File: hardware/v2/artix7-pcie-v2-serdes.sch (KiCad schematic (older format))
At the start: 23 parts, among them J4 USB3_A, J5 USB3_A_AS_PCIE, U1 XC7A75T-FGG484

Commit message: v2 hardware: add Digikey part numbers to schematic and generate bom
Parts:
- C19, C34: Vendor (none) -> 490-5915-1-ND
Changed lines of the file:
@@
 F 2 "tom-passives:C_0402_1005Metric" H 9638 5350 30  0001 C CNN
 F 3 "" H 9600 5500 60  0001 C CNN
+F 4 "490-5915-1-ND" H 9600 5500 50  0001 C CNN "Vendor"
 	1    9600 5500
 	1    0    0    -1
@@
 F 2 "tom-passives:C_0402_1005Metric" H 3338 5350 30  0001 C CNN
 F 3 "" H 3300 5500 60  0001 C CNN
+F 4 "490-5915-1-ND" H 3300 5500 50  0001 C CNN "Vendor"
 	1    3300 5500
 	1    0    0    -1

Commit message: hardware: add USB 3.0 connector digikey part number
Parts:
- J4, J5: Digikey (none) -> 2057-USB-A3-S-RA-ND
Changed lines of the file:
@@
 F 2 "tom-connectors:USB3_A_Aliexpress" H 2650 2350 50  0001 C CNN
 F 3 "~" H 2650 2350 50  0001 C CNN
+F 4 "2057-USB-A3-S-RA-ND" H 2500 2250 50  0001 C CNN "Digikey"
 	1    2500 2250
 	1    0    0    -1
@@
 F 2 "tom-connectors:USB3_A_Aliexpress" H 2650 4600 50  0001 C CNN
 F 3 "~" H 2650 4600 50  0001 C CNN
+F 4 "2057-USB-A3-S-RA-ND" H 2500 4500 50  0001 C CNN "Digikey"
 	1    2500 4500
 	1    0    0    -1

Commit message: v2 hardware: aug2020 pcb updates
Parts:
- removed R42, R44: DNP, tom-passives:R_0402_1005Metric_NoPaste, symbol tom-passives:R
- removed R43, R45: 0R, tom-passives:R_0402_1005Metric, symbol tom-passives:R
- added C3, C4: 0.1uF/6.3V/X5R, tom-passives:C_0402_1005Metric, symbol tom-passives:C
- R26, R27: value 0R -> 270R/5%
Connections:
- net S2_DRAIN is gone; now on net GND: J5.7 (DRAIN)
- net S2_GND is gone; now on net S2_PERST: J5.4 (GND)
- net GND: now also C3.2, C4.2
- net S2_RX_N: now also U1.B10 (MGTPRXP2_216); no longer U1.A10 (MGTPRXN2_216)
- net S2_RX_P: now also U1.A10 (MGTPRXN2_216); no longer U1.B10 (MGTPRXP2_216)
- net at J4.10 (SHIELD), R26.1: now also C3.1
- net at J5.10 (SHIELD), R27.1: now also C4.1
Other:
- note added: "P/N reversal on MGT2 RX"
- moved on the sheet: R26, R27
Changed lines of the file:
@@
 L tom-passives:R R26
 U 1 1 5EACE9C5
-P 2050 3050
-F 0 "R26" V 1865 3050 40  0000 C CNN
-F 1 "0R" V 1941 3050 40  0000 C CNN
-F 2 "tom-passives:R_0402_1005Metric" V 1980 3050 30  0001 C CNN
-F 3 "" H 2050 3050 30  0001 C CNN
-	1    2050 3050
-	0    1    1    0
+P 1500 3050
+F 0 "R26" V 1315 3050 40  0000 C CNN
+F 1 "270R/5%" V 1391 3050 40  0000 C CNN
+F 2 "tom-passives:R_0402_1005Metric" V 1430 3050 30  0001 C CNN
+F 3 "" H 1500 3050 30  0001 C CNN
+	1    1500 3050
+	0    1    -1   0
 $EndComp
 Wire Wire Line
@@
 L power:GND #PWR058
 U 1 1 5EACF99A
-P 1800 3050
-F 0 "#PWR058" H 1800 2800 50  0001 C CNN
-F 1 "GND" H 1805 2877 50  0000 C CNN
-F 2 "" H 1800 3050 50  0001 C CNN
-F 3 "" H 1800 3050 50  0001 C CNN
-	1    1800 3050
+P 1100 3050
+F 0 "#PWR058" H 1100 2800 50  0001 C CNN
+F 1 "GND" H 1105 2877 50  0000 C CNN
+F 2 "" H 1100 3050 50  0001 C CNN
+F 3 "" H 1100 3050 50  0001 C CNN
+	1    1100 3050
 	1    0    0    -1
 $EndComp
 Text HLabel 1700 5950 0    50   Output ~ 0
 S2_PERST
-Wire Wire Line
-	2300 5200 2300 5350
 $Comp
 L power:GND #PWR059
 U 1 1 5EAD2F17
-P 1800 5350
-F 0 "#PWR059" H 1800 5100 50  0001 C CNN
-F 1 "GND" H 1805 5177 50  0000 C CNN
-F 2 "" H 1800 5350 50  0001 C CNN
-F 3 "" H 1800 5350 50  0001 C CNN
-	1    1800 5350
+P 1700 5650
+F 0 "#PWR059" H 1700 5400 50  0001 C CNN
+F 1 "GND" H 1705 5477 50  0000 C CNN
+F 2 "" H 1700 5650 50  0001 C CNN
+F 3 "" H 1700 5650 50  0001 C CNN
+	1    1700 5650
 	1    0    0    -1
 $EndComp
@@
 L tom-passives:R R27
 U 1 1 5EAD1FF6
-P 2050 5350
-F 0 "R27" V 1865 5350 40  0000 C CNN
-F 1 "0R" V 1941 5350 40  0000 C CNN
-F 2 "tom-passives:R_0402_1005Metric" V 1980 5350 30  0001 C CNN
-F 3 "" H 2050 5350 30  0001 C CNN
-	1    2050 5350
+P 2000 5350
+F 0 "R27" V 1815 5350 40  0000 C CNN
+F 1 "270R/5%" V 1891 5350 40  0000 C CNN
+F 2 "tom-passives:R_0402_1005Metric" V 1930 5350 30  0001 C CNN
+F 3 "" H 2000 5350 30  0001 C CNN
+	1    2000 5350
 	0    1    1    0
-$EndComp
-$Comp
-L power:GND #PWR061
-U 1 1 5EACBD31
-P 3000 5950
-F 0 "#PWR061" H 3000 5700 50  0001 C CNN
-F 1 "GND" H 3005 5777 50  0000 C CNN
-F 2 "" H 3000 5950 50  0001 C CNN
-F 3 "" H 3000 5950 50  0001 C CNN
-	1    3000 5950
-	1    0    0    -1
 $EndComp
 Wire Wire Line
@@
 	1    0    0    -1
 $EndComp
-$Comp
-L tom-passives:R R44
-U 1 1 5F029E9A
-P 2750 5950
-F 0 "R44" V 2565 5950 40  0000 C CNN
-F 1 "DNP" V 2641 5950 40  0000 C CNN
-F 2 "tom-passives:R_0402_1005Metric_NoPaste" V 2680 5950 30  0001 C CNN
-F 3 "" H 2750 5950 30  0001 C CNN
-	1    2750 5950
-	0    1    1    0
-$EndComp
-$Comp
-L tom-passives:R R43
-U 1 1 5F02A201
-P 2150 5950
-F 0 "R43" V 1965 5950 40  0000 C CNN
-F 1 "0R" V 2041 5950 40  0000 C CNN
-F 2 "tom-passives:R_0402_1005Metric" V 2080 5950 30  0001 C CNN
-F 3 "" H 2150 5950 30  0001 C CNN
-	1    2150 5950
-	0    1    1    0
-$EndComp
 Wire Wire Line
 	2500 5200 2500 5950
 Wire Wire Line
-	2500 5950 2400 5950
-Connection ~ 2500 5950
-Wire Wire Line
-	1700 5950 1900 5950
-$Comp
-L tom-passives:R R42
-U 1 1 5F0598E8
-P 2150 5650
-F 0 "R42" V 1965 5650 40  0000 C CNN
-F 1 "DNP" V 2041 5650 40  0000 C CNN
-F 2 "tom-passives:R_0402_1005Metric_NoPaste" V 2080 5650 30  0001 C CNN
-F 3 "" H 2150 5650 30  0001 C CNN
-	1    2150 5650
-	0    1    1    0
-$EndComp
-Wire Wire Line
-	1900 5650 1900 5950
-Connection ~ 1900 5950
-Wire Wire Line
 	2400 5200 2400 5650
-$Comp
-L tom-passives:R R45
-U 1 1 5F07398D
-P 2850 5650
-F 0 "R45" V 2665 5650 40  0000 C CNN
-F 1 "0R" V 2741 5650 40  0000 C CNN
-F 2 "tom-passives:R_0402_1005Metric" V 2780 5650 30  0001 C CNN
-F 3 "" H 2850 5650 30  0001 C CNN
-	1    2850 5650
-	0    1    1    0
-$EndComp
 $Comp
 L power:GND #PWR035
 U 1 1 5F073E12
-P 3100 5650
-F 0 "#PWR035" H 3100 5400 50  0001 C CNN
-F 1 "GND" H 3105 5477 50  0000 C CNN
-F 2 "" H 3100 5650 50  0001 C CNN
-F 3 "" H 3100 5650 50  0001 C CNN
-	1    3100 5650
-	1    0    0    -1
-$EndComp
-Wire Wire Line
-	2600 5650 2400 5650
-Connection ~ 2400 5650
-$Comp
-L power:PWR_FLAG #FLG0114
-U 1 1 5F118316
-P 2600 5650
-F 0 "#FLG0114" H 2600 5725 50  0001 C CNN
-F 1 "PWR_FLAG" V 2600 5950 50  0000 C CNN
-F 2 "" H 2600 5650 50  0001 C CNN
-F 3 "~" H 2600 5650 50  0001 C CNN
-	1    2600 5650
-	1    0    0    -1
-$EndComp
-Connection ~ 2600 5650
-$Comp
-L power:PWR_FLAG #FLG0115
-U 1 1 5F11842A
-P 2400 5950
-F 0 "#FLG0115" H 2400 6025 50  0001 C CNN
-F 1 "PWR_FLAG" H 2400 6123 50  0000 C CNN
-F 2 "" H 2400 5950 50  0001 C CNN
-F 3 "~" H 2400 5950 50  0001 C CNN
-	1    2400 5950
-	-1   0    0    1
-$EndComp
-Connection ~ 2400 5950
+P 2400 5650
+F 0 "#PWR035" H 2400 5400 50  0001 C CNN
+F 1 "GND" H 2405 5477 50  0000 C CNN
+F 2 "" H 2400 5650 50  0001 C CNN
+F 3 "" H 2400 5650 50  0001 C CNN
+	1    2400 5650
+	1    0    0    -1
+$EndComp
 NoConn ~ 7250 2000
 NoConn ~ 7250 2100
-Wire Wire Line
-	4300 3200 7250 3200
-Wire Wire Line
-	7250 3100 4400 3100
 Wire Wire Line
 	7250 2300 5400 2300
@@
 Wire Wire Line
 	8900 5700 9100 5700
-Text Label 2500 5600 1    50   ~ 0
-S2_GND
-Text Label 2400 5600 1    50   ~ 0
-S2_DRAIN
 Wire Wire Line
 	3100 3500 1900 3500
@@
 	7150 3000 7150 3300
 Wire Wire Line
-	4300 3200 4300 4600
-Wire Wire Line
-	4400 3100 4400 4700
+	4300 3100 4300 4600
+Wire Wire Line
+	4400 3200 4400 4700
 Wire Wire Line
 	7250 3300 7150 3300
@@
 NoConn ~ 7250 2400
 NoConn ~ 7250 2500
+Wire Wire Line
+	1700 5950 2500 5950
+Wire Wire Line
+	4400 3200 7250 3200
+Wire Wire Line
+	7250 3100 4300 3100
+Text Label 6650 3100 0    50   ~ 0
+S2_RX_N
+Text Label 6650 3200 0    50   ~ 0
+S2_RX_P
+Text Notes 6100 3000 0    50   ~ 0
+P/N reversal on MGT2 RX
+$Comp
+L tom-passives:C C4
+U 1 1 5F73BB56
+P 2000 5550
+F 0 "C4" V 2100 5400 40  0000 L CNN
+F 1 "0.1uF/6.3V/X5R" V 2200 5300 40  0000 L CNN
+F 2 "tom-passives:C_0402_1005Metric" H 2038 5400 30  0001 C CNN
+F 3 "" H 2000 5550 60  0001 C CNN
+	1    2000 5550
+	0    1    1    0
+$EndComp
+Wire Wire Line
+	2300 5550 2200 5550
+Wire Wire Line
+	1750 5350 1700 5350
+Wire Wire Line
+	1700 5350 1700 5550
+Wire Wire Line
+	1800 5550 1700 5550
+Connection ~ 1700 5550
+Wire Wire Line
+	1700 5550 1700 5650
+Wire Wire Line
+	2300 5200 2300 5350
+Wire Wire Line
+	2250 5350 2300 5350
+Connection ~ 2300 5350
+Wire Wire Line
+	2300 5350 2300 5550
+Wire Wire Line
+	2300 3050 1750 3050
+Wire Wire Line
+	1700 2750 1750 2750
+Wire Wire Line
+	1750 2750 1750 3050
+Connection ~ 1750 3050
+Wire Wire Line
+	1300 2750 1250 2750
+Wire Wire Line
+	1250 2750 1250 3050
+Wire Wire Line
+	1250 3050 1100 3050
+Connection ~ 1250 3050
+$Comp
+L tom-passives:C C3
+U 1 1 5F763D00
+P 1500 2750
+F 0 "C3" V 1600 2600 40  0000 L CNN
+F 1 "0.1uF/6.3V/X5R" V 1700 2500 40  0000 L CNN
+F 2 "tom-passives:C_0402_1005Metric" H 1538 2600 30  0001 C CNN
+F 3 "" H 1500 2750 60  0001 C CNN
+	1    1500 2750
+	0    1    -1   0
+$EndComp
 $EndSCHEMATC

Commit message: v2 hardware: Aug2020/rc2 version - flip tx/rx pairs on s2 - add lcsc part numbers
rc2 errata schematic
- change serial port connector to add +3.3V ? (8-pin)(NO)
- add test points for flash pre-programming
- smaller package on input direction diodes (NO)
- bom dupe errors
- remove all p/s 0R bringup parts
- optimise bom (use 1.5k for led, 10k/4.7k for i2c pullups)
- done led is bright (change to 4.7k)
- improve shield grounding with RC
- check actual values of RGB resistors
- remove caps from clock inputs

rc2 errata pcb
- no gnd marking on serial port connector pins
- change serial port connector to add +3.3V ? (8-pin) (NO)
- no test points for flash pre-programming
- missing caps on xtal? (No but select xtal carefully)
- Cfg sel pins on clock chip?
- No silk on test points
- No +/- pair numbering on silk
- vcc test points for clk pre-programming? (or use bootloader)
- random silk circle under S2
- smaller package on input direction diodes (NO)
- no polarity on 100uF tantalum
- some via in or close to pads
- wrong button package (change from feather to chinese)
- gnd/vcc labels swapped at high end of J2
- clock chip OUT0_SEL_I2CB needs to be tied high after programming
- check teardrops
- power diode footprint marking reverse
- LEDs use cap footprint
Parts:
- C19, C34: LCSC (none) -> C23733
- C20, C21, C22, C24, C26, C28, C3, C30, C32, C33, C4, C47, C48: LCSC (none) -> C1525
- J4, J5, U1: LCSC (none) -> DNP
- R26, R27: LCSC (none) -> C25099
- R28: LCSC (none) -> C25076
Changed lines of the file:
@@
 F 2 "artix7-pcie-v2:Xilinx_FGG484" H 8750 2900 50  0001 C CNN
 F 3 "" H 8750 2900 50  0000 C CNN
+F 4 "DNP" H 8750 2900 50  0001 C CNN "LCSC"
 	4    8750 2900
 	1    0    0    -1
@@
 F 3 "~" H 2650 2350 50  0001 C CNN
 F 4 "2057-USB-A3-S-RA-ND" H 2500 2250 50  0001 C CNN "Digikey"
+F 5 "DNP" H 2500 2250 50  0001 C CNN "LCSC"
 	1    2500 2250
 	1    0    0    -1
@@
 F 2 "tom-passives:C_0402_1005Metric" H 5738 1650 30  0001 C CNN
 F 3 "" H 5700 1800 60  0001 C CNN
+F 4 "C1525" H 5700 1800 50  0001 C CNN "LCSC"
 	1    5700 1800
 	0    1    1    0
@@
 F 2 "tom-passives:C_0402_1005Metric" H 6238 1750 30  0001 C CNN
 F 3 "" H 6200 1900 60  0001 C CNN
+F 4 "C1525" H 6200 1900 50  0001 C CNN "LCSC"
 	1    6200 1900
 	0    1    1    0
@@
 F 2 "tom-passives:R_0402_1005Metric" V 1430 3050 30  0001 C CNN
 F 3 "" H 1500 3050 30  0001 C CNN
+F 4 "C25099" H 1500 3050 50  0001 C CNN "LCSC"
 	1    1500 3050
 	0    1    -1   0
@@
 F 2 "tom-passives:R_0402_1005Metric" V 1930 5350 30  0001 C CNN
 F 3 "" H 2000 5350 30  0001 C CNN
+F 4 "C25099" H 2000 5350 50  0001 C CNN "LCSC"
 	1    2000 5350
 	0    1    1    0
@@
 F 2 "artix7-pcie-v2:Xilinx_FGG484" H 6550 5700 50  0001 C CNN
 F 3 "" H 6550 5700 50  0000 C CNN
+F 4 "DNP" H 6550 5700 50  0001 C CNN "LCSC"
 	5    6550 5700
 	1    0    0    -1
@@
 F 2 "tom-passives:R_0402_1005Metric" V 8280 6000 30  0001 C CNN
 F 3 "" H 8350 6000 30  0001 C CNN
+F 4 "C25076" H 8350 6000 50  0001 C CNN "LCSC"
 	1    8350 6000
 	0    -1   1    0
@@
 F 2 "tom-passives:C_0402_1005Metric" H 8938 5350 30  0001 C CNN
 F 3 "" H 8900 5500 60  0001 C CNN
+F 4 "C1525" H 8900 5500 50  0001 C CNN "LCSC"
 	1    8900 5500
 	1    0    0    -1
@@
 F 2 "tom-passives:C_0402_1005Metric" H 9338 5350 30  0001 C CNN
 F 3 "" H 9300 5500 60  0001 C CNN
+F 4 "C1525" H 9300 5500 50  0001 C CNN "LCSC"
 	1    9300 5500
 	1    0    0    -1
@@
 F 2 "tom-passives:C_0402_1005Metric" H 9138 5350 30  0001 C CNN
 F 3 "" H 9100 5500 60  0001 C CNN
+F 4 "C1525" H 9100 5500 50  0001 C CNN "LCSC"
 	1    9100 5500
 	1    0    0    -1
@@
 F 3 "" H 9600 5500 60  0001 C CNN
 F 4 "490-5915-1-ND" H 9600 5500 50  0001 C CNN "Vendor"
+F 5 "C23733" H 9600 5500 50  0001 C CNN "LCSC"
 	1    9600 5500
 	1    0    0    -1
@@
 F 2 "tom-passives:C_0402_1005Metric" H 4388 5350 30  0001 C CNN
 F 3 "" H 4350 5500 60  0001 C CNN
+F 4 "C1525" H 4350 5500 50  0001 C CNN "LCSC"
 	1    4350 5500
 	1    0    0    -1
@@
 F 2 "tom-passives:C_0402_1005Metric" H 4088 5350 30  0001 C CNN
 F 3 "" H 4050 5500 60  0001 C CNN
+F 4 "C1525" H 4050 5500 50  0001 C CNN "LCSC"
 	1    4050 5500
 	1    0    0    -1
@@
 F 3 "" H 3300 5500 60  0001 C CNN
 F 4 "490-5915-1-ND" H 3300 5500 50  0001 C CNN "Vendor"
+F 5 "C23733" H 3300 5500 50  0001 C CNN "LCSC"
 	1    3300 5500
 	1    0    0    -1
@@
 F 2 "tom-passives:C_0402_1005Metric" H 4738 2050 30  0001 C CNN
 F 3 "" H 4700 2200 60  0001 C CNN
+F 4 "C1525" H 4700 2200 50  0001 C CNN "LCSC"
 	1    4700 2200
 	0    1    1    0
@@
 F 2 "tom-passives:C_0402_1005Metric" H 5238 2150 30  0001 C CNN
 F 3 "" H 5200 2300 60  0001 C CNN
+F 4 "C1525" H 5200 2300 50  0001 C CNN "LCSC"
 	1    5200 2300
 	0    1    1    0
@@
 F 3 "~" H 2650 4600 50  0001 C CNN
 F 4 "2057-USB-A3-S-RA-ND" H 2500 4500 50  0001 C CNN "Digikey"
+F 5 "DNP" H 2500 4500 50  0001 C CNN "LCSC"
 	1    2500 4500
 	1    0    0    -1
@@
 F 2 "tom-passives:C_0402_1005Metric" H 5688 3750 30  0001 C CNN
 F 3 "" H 5650 3900 60  0001 C CNN
+F 4 "C1525" H 5650 3900 50  0001 C CNN "LCSC"
 	1    5650 3900
 	0    1    -1   0
@@
 F 2 "tom-passives:C_0402_1005Metric" H 5188 3650 30  0001 C CNN
 F 3 "" H 5150 3800 60  0001 C CNN
+F 4 "C1525" H 5150 3800 50  0001 C CNN "LCSC"
 	1    5150 3800
 	0    1    -1   0
@@
 F 2 "tom-passives:C_0402_1005Metric" H 2038 5400 30  0001 C CNN
 F 3 "" H 2000 5550 60  0001 C CNN
+F 4 "C1525" H 2000 5550 50  0001 C CNN "LCSC"
 	1    2000 5550
 	0    1    1    0
@@
 F 2 "tom-passives:C_0402_1005Metric" H 1538 2600 30  0001 C CNN
 F 3 "" H 1500 2750 60  0001 C CNN
+F 4 "C1525" H 1500 2750 50  0001 C CNN "LCSC"
 	1    1500 2750
 	0    1    -1   0

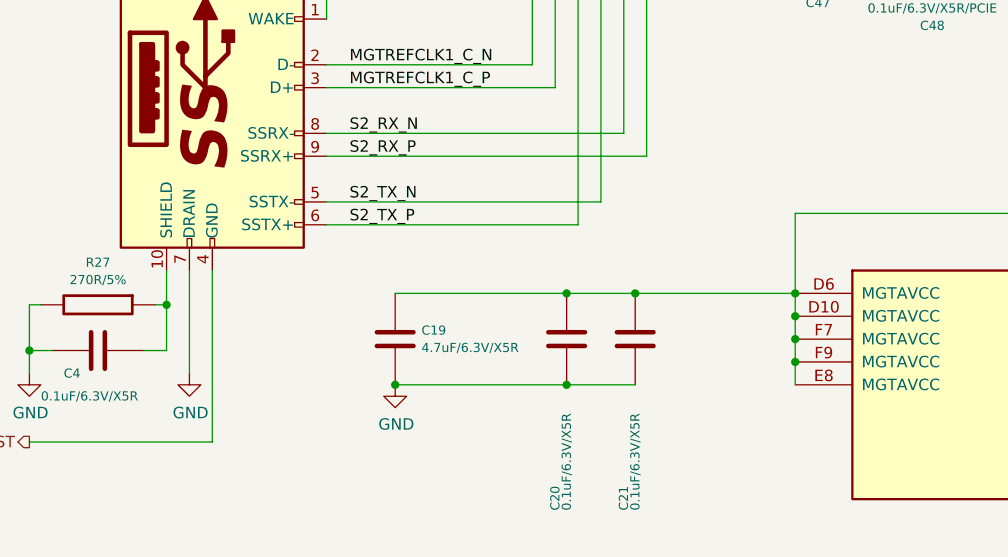
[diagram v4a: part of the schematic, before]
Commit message: JLC power supplies almost routed VCCBRAM to go Need to - check BOM - add power good leds - fix vccbram inc caps - fix 100uF part number - update silk
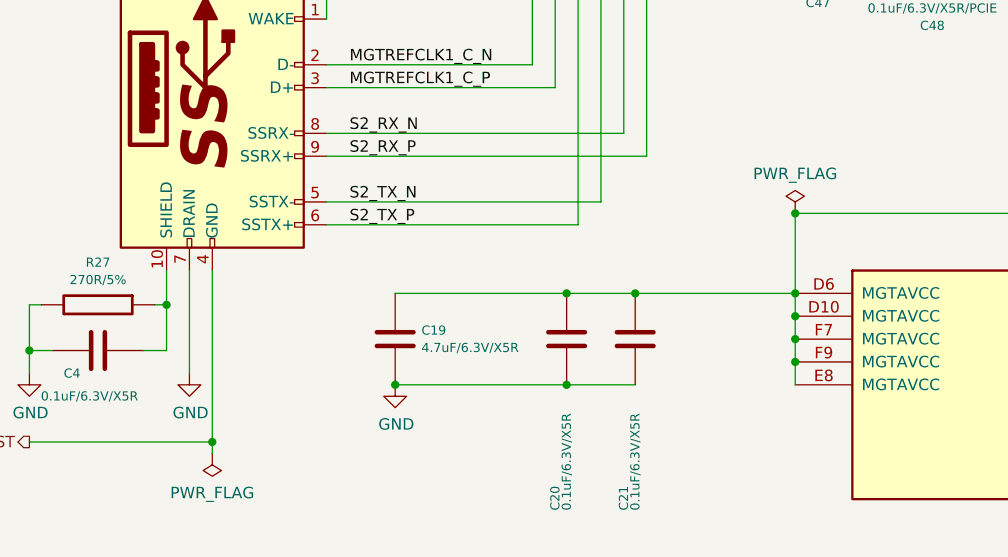
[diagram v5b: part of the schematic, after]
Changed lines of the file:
@@
 	0    1    -1   0
 $EndComp
+$Comp
+L power:PWR_FLAG #FLG0103
+U 1 1 5F92DBE7
+P 5050 4950
+F 0 "#FLG0103" H 5050 5025 50  0001 C CNN
+F 1 "PWR_FLAG" H 5050 5123 50  0000 C CNN
+F 2 "" H 5050 4950 50  0001 C CNN
+F 3 "~" H 5050 4950 50  0001 C CNN
+	1    5050 4950
+	1    0    0    -1
+$EndComp
+Connection ~ 5050 4950
+$Comp
+L power:PWR_FLAG #FLG0107
+U 1 1 5F935D96
+P 2500 6000
+F 0 "#FLG0107" H 2500 6075 50  0001 C CNN
+F 1 "PWR_FLAG" H 2500 6173 50  0000 C CNN
+F 2 "" H 2500 6000 50  0001 C CNN
+F 3 "~" H 2500 6000 50  0001 C CNN
+	1    2500 6000
+	-1   0    0    1
+$EndComp
+Wire Wire Line
+	2500 6000 2500 5950
+Connection ~ 2500 5950
 $EndSCHEMATC

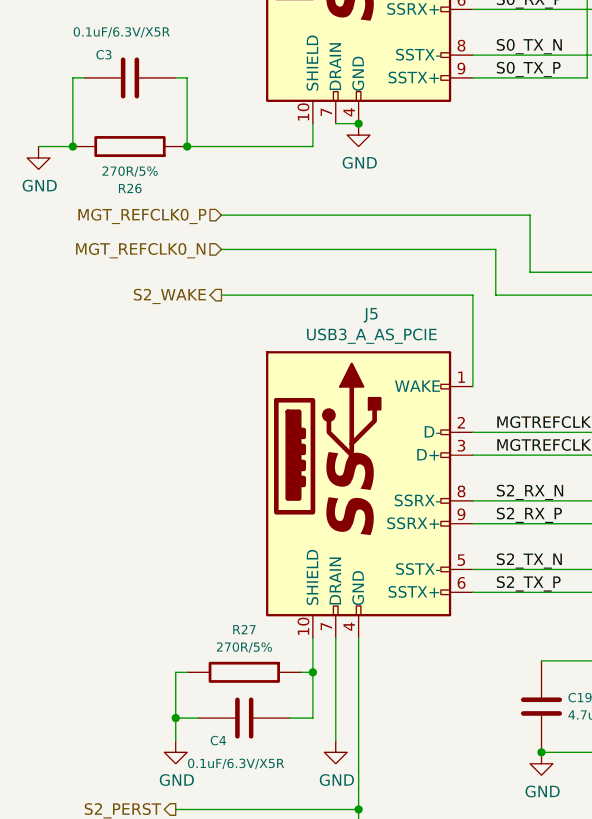
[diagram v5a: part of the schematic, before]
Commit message: v2 hardware updates: fixed inductor footprint, updates for DFA
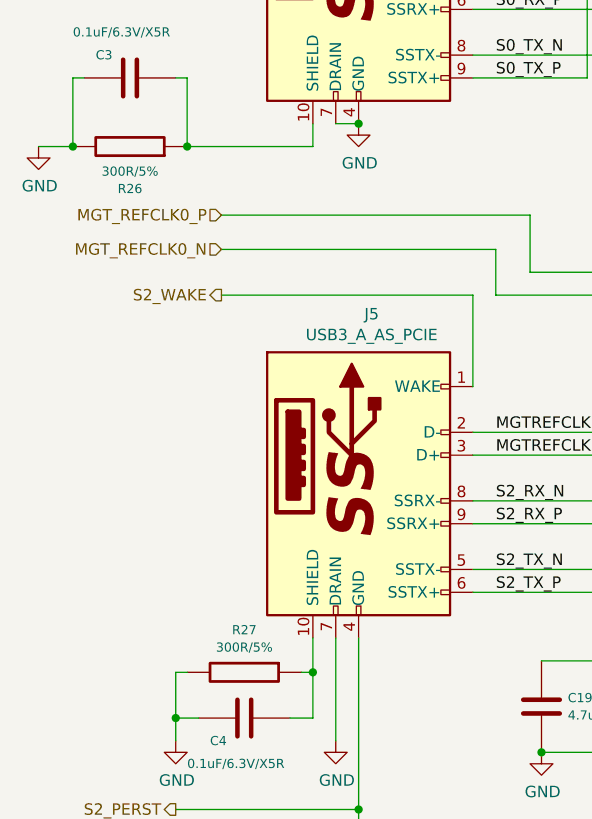
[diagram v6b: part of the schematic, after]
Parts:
- R26, R27: value 270R/5% -> 300R/5%; LCSC C25099 -> C25102
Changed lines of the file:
@@
 P 1500 3050
 F 0 "R26" V 1315 3050 40  0000 C CNN
-F 1 "270R/5%" V 1391 3050 40  0000 C CNN
+F 1 "300R/5%" V 1391 3050 40  0000 C CNN
 F 2 "tom-passives:R_0402_1005Metric" V 1430 3050 30  0001 C CNN
 F 3 "" H 1500 3050 30  0001 C CNN
-F 4 "C25099" H 1500 3050 50  0001 C CNN "LCSC"
+F 4 "C25102" H 1500 3050 50  0001 C CNN "LCSC"
 	1    1500 3050
 	0    1    -1   0
@@
 P 2000 5350
 F 0 "R27" V 1815 5350 40  0000 C CNN
-F 1 "270R/5%" V 1891 5350 40  0000 C CNN
+F 1 "300R/5%" V 1891 5350 40  0000 C CNN
 F 2 "tom-passives:R_0402_1005Metric" V 1930 5350 30  0001 C CNN
 F 3 "" H 2000 5350 30  0001 C CNN
-F 4 "C25099" H 2000 5350 50  0001 C CNN "LCSC"
+F 4 "C25102" H 2000 5350 50  0001 C CNN "LCSC"
 	1    2000 5350
 	0    1    1    0
